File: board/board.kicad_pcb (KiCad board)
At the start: 4 copper layers, 21 x 126 mm, 65 parts, among them IC1 RTL8305NB-CG, J1 001_I2C, J2 019_100BASE-T_with_CT, J3 019_100BASE-T_with_CT, J4 019_100BASE-T_with_CT, J5 019_100BASE-T_with_CT, J6 019_100BASE-T_with_CT, J7 019_100BASE-T_with_CT, J8 019_100BASE-T_with_CT, J9 019_100BASE-T_with_CT, Y1 25Mhz

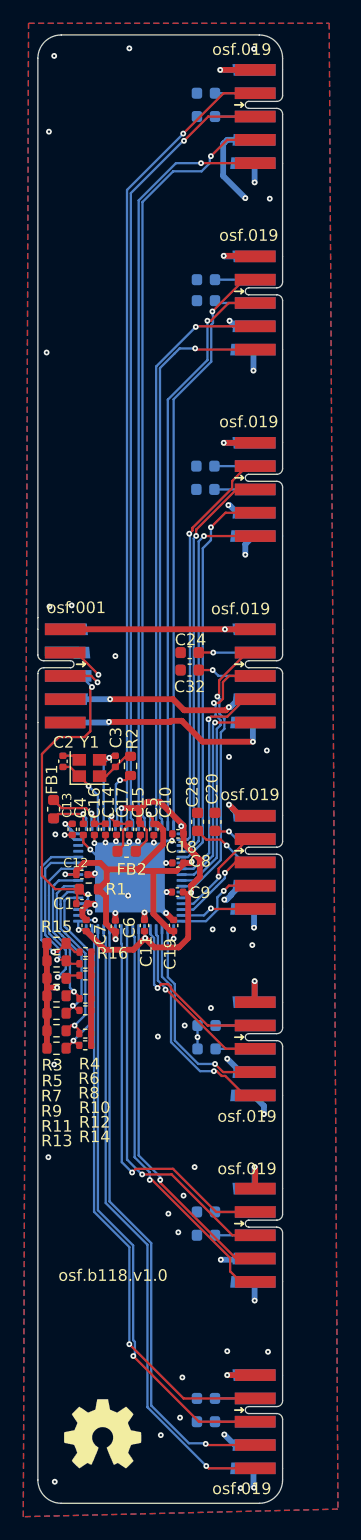
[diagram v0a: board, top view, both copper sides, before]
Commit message: added N filter for input voltage
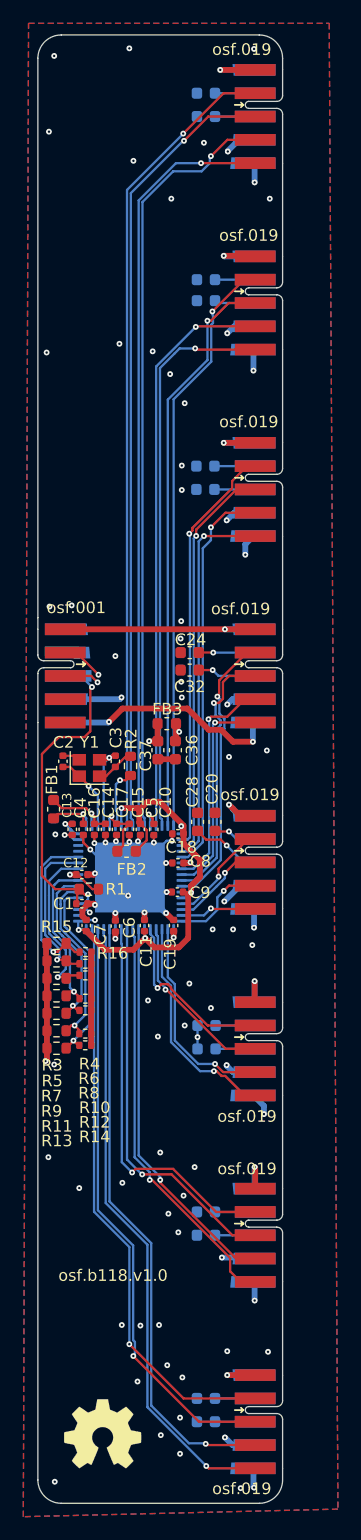
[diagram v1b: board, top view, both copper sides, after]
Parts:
- added C36: 10uF, Capacitor_SMD:C_0603_1608Metric, F.Cu at (151.8, 103.4)
- added C37: 10uF, Capacitor_SMD:C_0603_1608Metric, F.Cu at (150.3, 103.4)
- added FB3: 0R, Inductor_SMD:L_0603_1608Metric, F.Cu at (151.1, 101.1)
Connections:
- C10 pad 1: +3.3V -> /sw_vcc
- C12 pad 1: +3.3V -> /sw_vcc
- C19 pad 1: +3.3V -> /sw_vcc
- C4 pad 1: +3.3V -> /sw_vcc
- C6 pad 1: +3.3V -> /sw_vcc
- C8 pad 1: +3.3V -> /sw_vcc
- FB1 pad 1: +3.3V -> /sw_vcc
- IC1 pad 17: +3.3V -> /sw_vcc
- IC1 pad 27: +3.3V -> /sw_vcc
- IC1 pad 41: +3.3V -> /sw_vcc
- IC1 pad 49: +3.3V -> /sw_vcc
- IC1 pad 6: +3.3V -> /sw_vcc
- IC1 pad 60: +3.3V -> /sw_vcc
- R1 pad 1: +3.3V -> /sw_vcc
- R11 pad 1: +3.3V -> /sw_vcc
- R13 pad 1: +3.3V -> /sw_vcc
- R15 pad 1: +3.3V -> /sw_vcc
- R3 pad 1: +3.3V -> /sw_vcc
- R5 pad 1: +3.3V -> /sw_vcc
- R7 pad 1: +3.3V -> /sw_vcc
- R9 pad 1: +3.3V -> /sw_vcc
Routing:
- net +3.3V: track 216.0 -> 152.6 mm, vias 16 -> 10
- net /sw_vcc: track 0.00 -> 26.3 mm, vias 0 -> 8
- net GND: track 138.4 -> 139.9 mm, vias 57 -> 81
- net +5V: track 152.6 -> 153.5 mm
- added copper zone on In1.Cu, net /sw_vcc
- removed copper zone on In1.Cu, net +3.3V

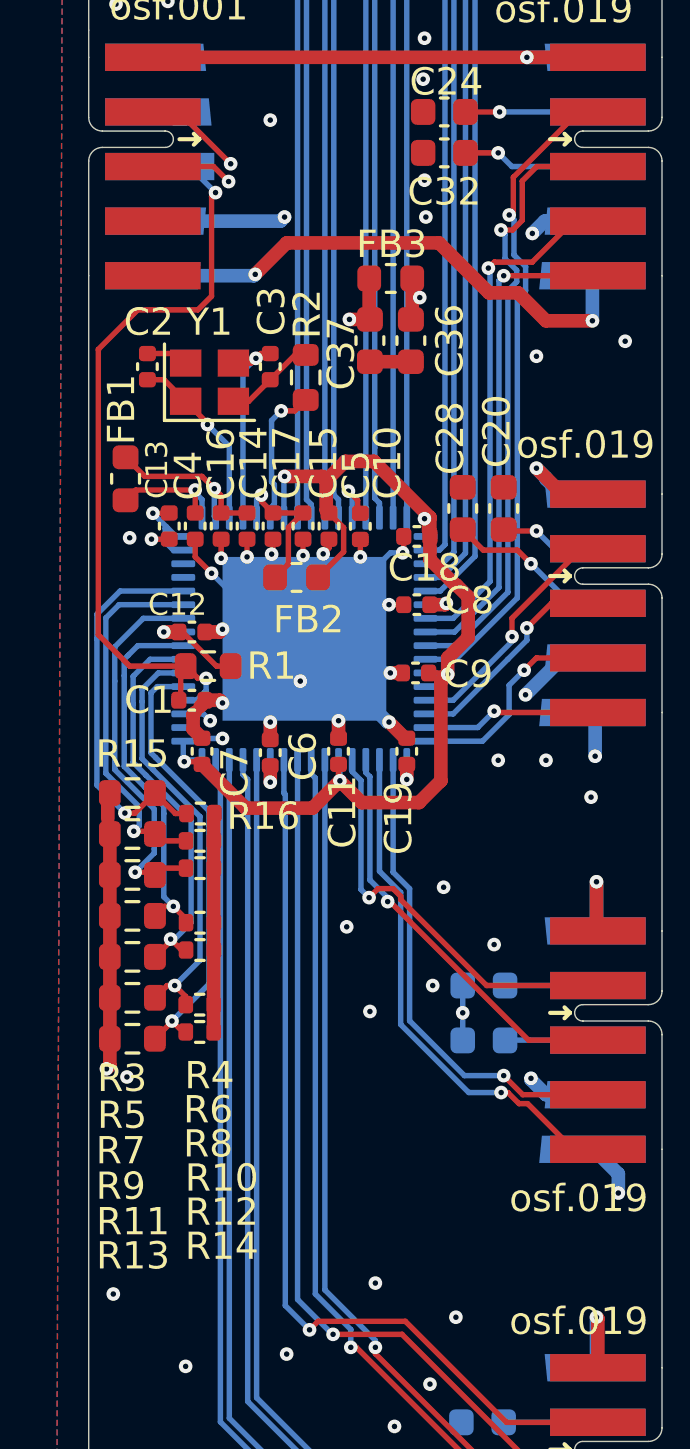
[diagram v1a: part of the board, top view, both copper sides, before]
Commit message: added lcsc numbers and updated I2C connector
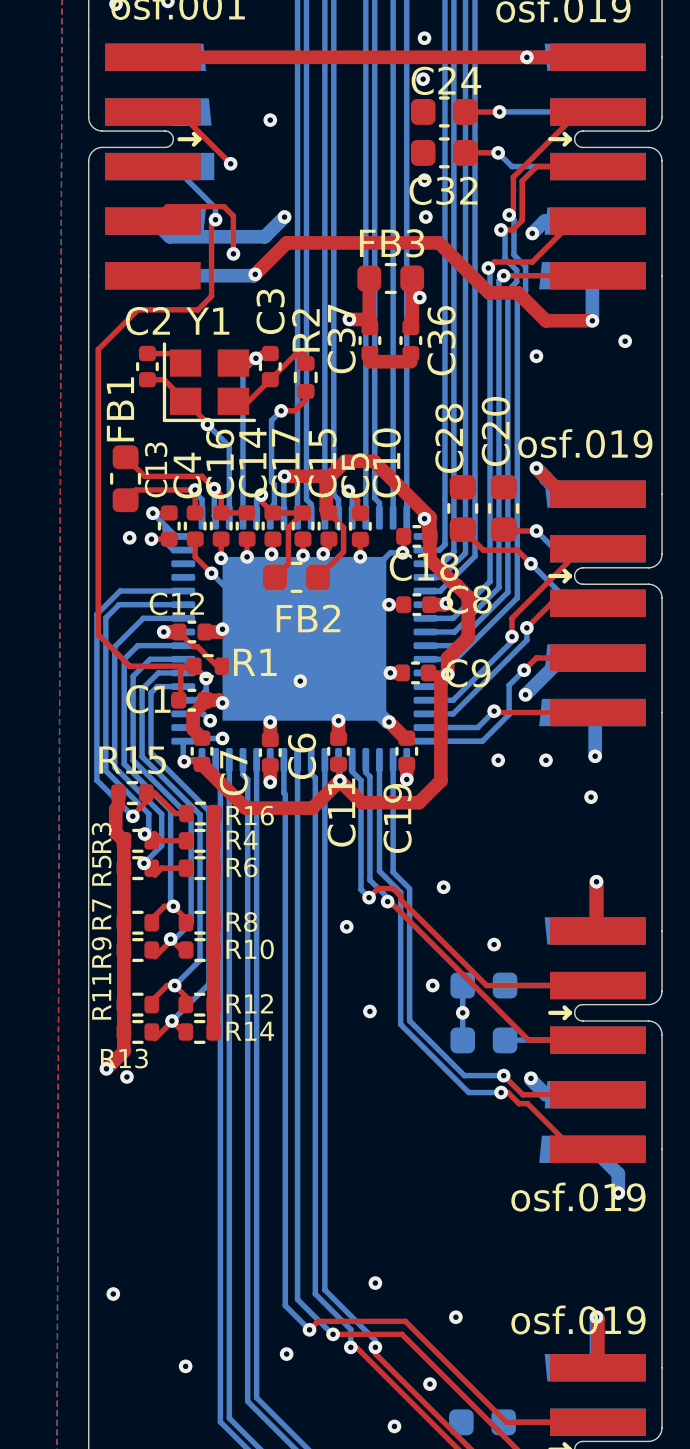
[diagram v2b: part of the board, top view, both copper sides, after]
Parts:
- C36, C37: footprint Capacitor_SMD:C_0603_1608Metric -> Capacitor_SMD:C_0402_1005Metric
- FB1, FB2: value Ferrite_Bead_Small -> 0R
- R1, R11, R13, R15, R2, R3, R5, R7, R9: footprint Resistor_SMD:R_0603_1608Metric -> Resistor_SMD:R_0402_1005Metric
- moved R11 0.32 mm to (141.8, 127.7)
- moved R13 0.32 mm to (141.8, 128.7)
- moved R3 0.32 mm to (141.8, 121.7)
- moved R5 0.32 mm to (141.8, 122.7)
- moved R7 0.32 mm to (141.8, 124.7)
- moved R9 0.32 mm to (141.8, 125.7)
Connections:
- J1 pad 3: /switch/SCL -> unconnected-(J1-N/C-Pad3)
- J1 pad 4: unconnected-(J1-Pad4) -> /switch/SCL
- J1 pad 6: (no net) -> unconnected-(J1-CS/EN-Pad6)
- J1 pad 7: (no net) -> unconnected-(J1-status-Pad7)
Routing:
- net /switch/SCL: track 29.9 -> 29.0 mm
- net /sw_vcc: track 26.3 -> 26.9 mm
